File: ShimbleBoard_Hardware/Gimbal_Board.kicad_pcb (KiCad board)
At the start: 2 copper layers, 124.5 x 94 mm, 85 parts, among them Q1 Q_NMOS_GDS, Q2 Q_NMOS_GDS, Q3 Q_NMOS_GDS, Q4 Q_NMOS_GDS, Q5 Q_NMOS_GDS, Q6 Q_NMOS_GDS, Q7 Q_NMOS_GDS, Q8 Q_NMOS_GDS, SW1 SW_Push, SW10 SW_SPDT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

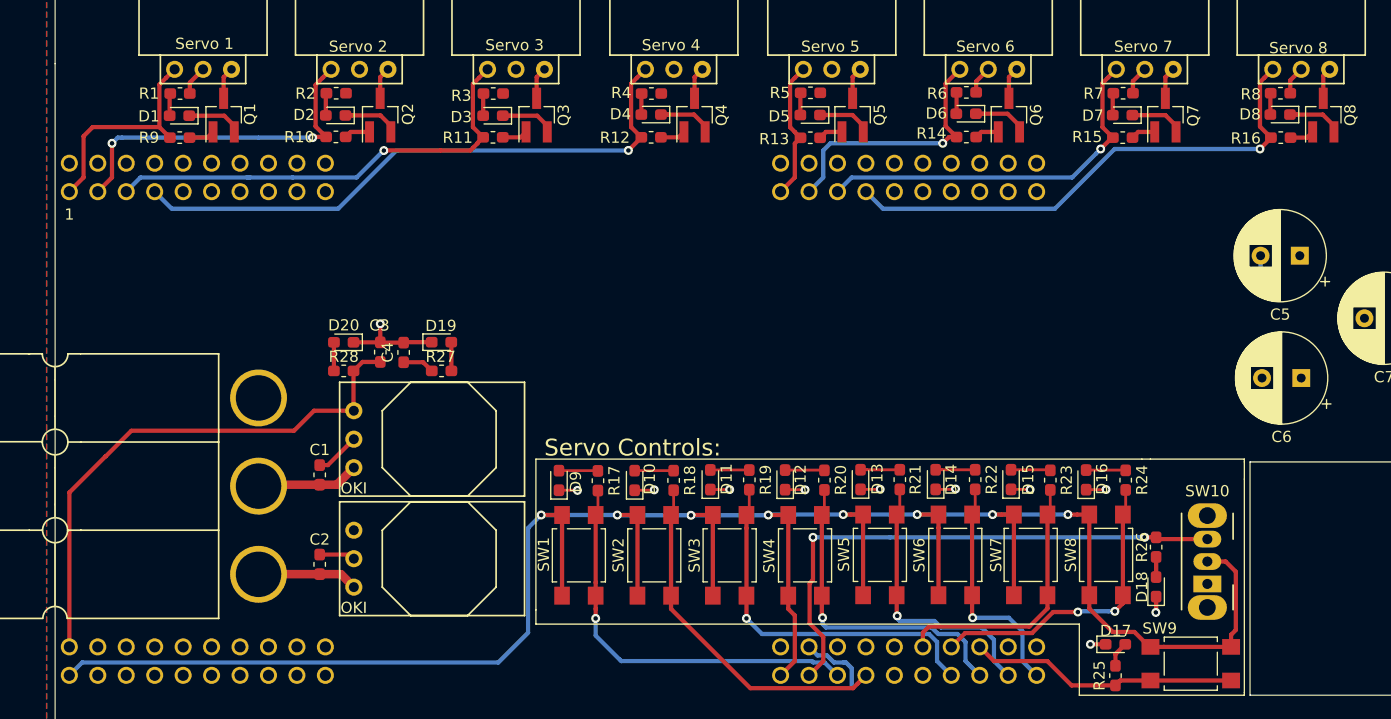
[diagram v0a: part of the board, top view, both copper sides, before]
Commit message: Changed the LED's to 5VL and fixed the wiring for it and added X's
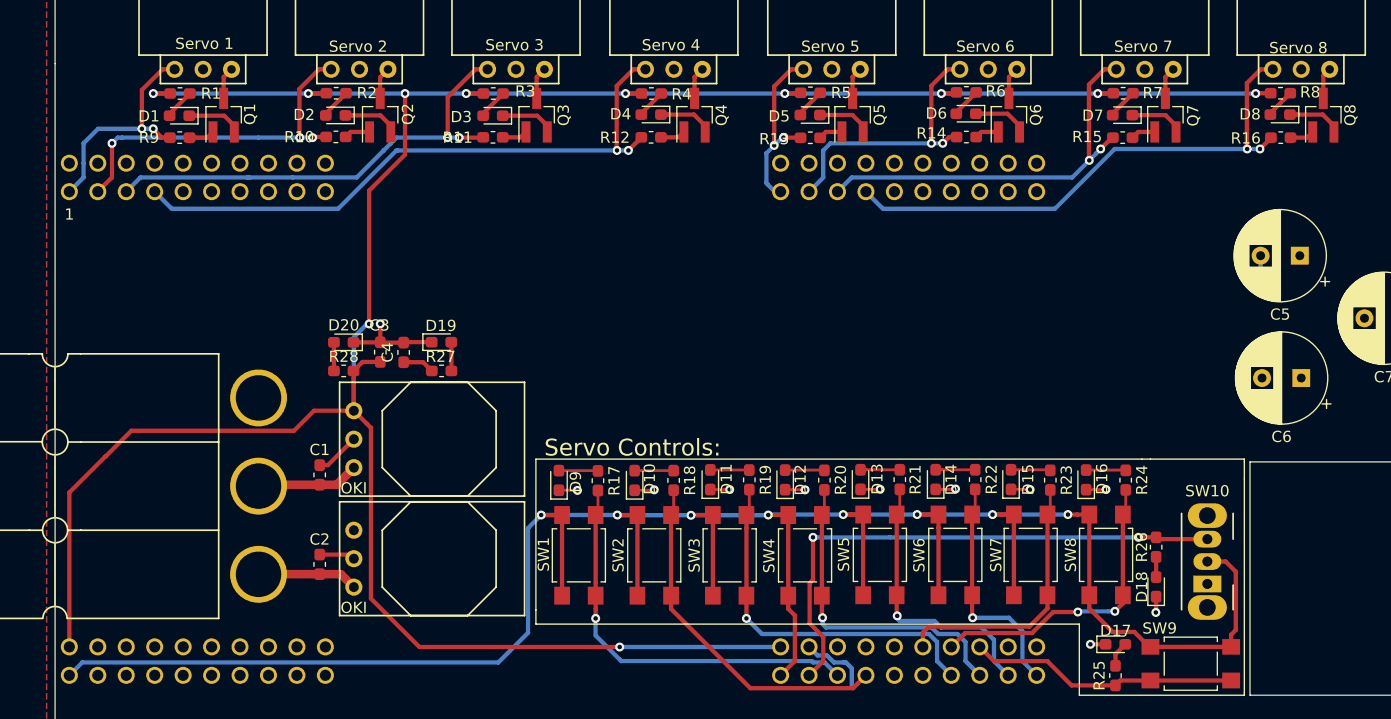
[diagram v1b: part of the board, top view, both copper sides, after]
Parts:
- U1: footprint MRDT_Shields:TM4C129E_Launchpad_FULL_THT_BOTTOM_5 -> MRDT_Shields:TM4C129E_Launchpad_FULL_THT_BOTTOM
- turned R1 to 0 degrees
- turned R2 to 0 degrees
- turned R3 to 0 degrees
- turned R4 to 0 degrees
- turned R5 to 0 degrees
- turned R6 to 0 degrees
- turned R7 to 0 degrees
- turned R8 to 0 degrees
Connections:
- R1 pad 1: +5VA -> +5VL
- R2 pad 1: +5VA -> +5VL
- R3 pad 1: +5VA -> +5VL
- R4 pad 1: +5VA -> +5VL
- R5 pad 1: +5VA -> +5VL
- R6 pad 1: +5VA -> +5VL
- R7 pad 1: +5VA -> +5VL
- R8 pad 1: +5VA -> +5VL
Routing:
- net +5VL: track 48.8 -> 245.1 mm, vias 0 -> 11
- net +5VA: track 13.1 -> 2.84 mm
- net Servo_Ctrl_5: track 12.5 -> 16.4 mm, vias 0 -> 2
- net Servo_Ctrl_7: track 33.6 -> 36.4 mm, vias 1 -> 2
- net Servo_Ctrl_4: track 53.7 -> 55.7 mm, vias 1 -> 2
- net Servo_Ctrl_8: track 46.4 -> 48.2 mm, vias 1 -> 2
- net Servo_Ctrl_6: track 23.6 -> 24.9 mm, vias 1 -> 2
- net Servo_Ctrl_3: track 41.1 -> 42.3 mm, vias 1 -> 2
- net Servo_Ctrl_1: track 19.6 -> 20.6 mm, vias 0 -> 2
- net Servo_Ctrl_2: track 31.2 -> 32.1 mm, vias 2 -> 3
- net Net-(D8-Pad2): track 1.92 -> 2.64 mm
- net Net-(D5-Pad2): track 1.99 -> 2.72 mm
- net Net-(D4-Pad2): track 1.89 -> 2.61 mm
- net Net-(D3-Pad2): track 1.99 -> 2.72 mm
- net Net-(D2-Pad2): track 2.00 -> 2.73 mm
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
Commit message: All but a bit
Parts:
- added D21: 12V_Log_LED, Diode_SMD:D_0603_1608Metric_Pad1.05x0.95mm_HandSolder, F.Cu at (93.2, 69.7)
- added D22: 12V_Act_LED, Diode_SMD:D_0603_1608Metric_Pad1.05x0.95mm_HandSolder, F.Cu at (101.9, 69.6)
- added R29: 1000, Resistor_SMD:R_0603_1608Metric_Pad1.05x0.95mm_HandSolder, F.Cu at (93.1, 72.5)
- added R30: 1000, Resistor_SMD:R_0603_1608Metric_Pad1.05x0.95mm_HandSolder, F.Cu at (101.9, 72.4)
- R17, R18, R19, R20, R21, R22, R23, R24, R25, R26: value 500 -> 330
- U1: footprint MRDT_Shields:TM4C129E_Launchpad_FULL_THT_BOTTOM -> MRDT_Shields:TM4C129E_Launchpad_FULL_THT_BOTTOM_5
- moved C4 1.78 mm to (98.4, 76.1)
- moved C3 1.78 mm to (96.3, 76.0)
- moved D19 1.78 mm to (101.8, 75.2)
- moved D20 1.78 mm to (93.1, 75.2)
- moved R27 1.78 mm to (101.8, 77.7)
- moved R28 1.78 mm to (93.1, 77.7)
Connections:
- Conn1 pad 1: Servo_Ctrl_1 -> +5VA
- Conn1 pad 2: +5VA -> GND
- Conn1 pad 3: GND -> Servo_Ctrl_1
- Conn2 pad 1: Servo_Ctrl_2 -> +5VA
- Conn2 pad 2: +5VA -> GND
- Conn2 pad 3: GND -> Servo_Ctrl_2
- Conn3 pad 1: Servo_Ctrl_3 -> +5VA
- Conn3 pad 2: +5VA -> GND
- Conn3 pad 3: GND -> Servo_Ctrl_3
- Conn4 pad 1: Servo_Ctrl_4 -> +5VA
- Conn4 pad 2: +5VA -> GND
- Conn4 pad 3: GND -> Servo_Ctrl_4
- Conn5 pad 1: Servo_Ctrl_5 -> +5VA
- Conn5 pad 2: +5VA -> GND
- Conn5 pad 3: GND -> Servo_Ctrl_5
- Conn6 pad 1: Servo_Ctrl_6 -> +5VA
- Conn6 pad 2: +5VA -> GND
- Conn6 pad 3: GND -> Servo_Ctrl_6
- Conn7 pad 1: Servo_Ctrl_7 -> +5VA
- Conn7 pad 2: +5VA -> GND
- Conn7 pad 3: GND -> Servo_Ctrl_7
- Conn8 pad 1: Servo_Ctrl_8 -> +5VA
- Conn8 pad 2: +5VA -> GND
- Conn8 pad 3: GND -> Servo_Ctrl_8
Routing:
- net +5VL: track 245.1 -> 191.1 mm, vias 11 -> 10
- net +5VA: track 2.84 -> 40.9 mm, vias 0 -> 9
- net +12VA: track 9.03 -> 44.4 mm, vias 0 -> 1
- net +12L: track 9.55 -> 31.1 mm, vias 0 -> 1
- net GND: track 63.5 -> 76.3 mm, vias 11 -> 14
- net Servo_Ctrl_1: track 20.6 -> 29.0 mm, vias 2 -> 1
- net Servo_Ctrl_3: track 42.3 -> 49.8 mm
- net Servo_Ctrl_4: track 55.7 -> 63.1 mm
- net Servo_Ctrl_2: track 32.1 -> 39.5 mm
- net Servo_Ctrl_7: track 36.4 -> 43.6 mm
- net Servo_Ctrl_8: track 48.2 -> 55.4 mm
- net Servo_Ctrl_6: track 24.9 -> 32.2 mm
- net Servo_Ctrl_5: track 16.4 -> 23.5 mm, vias 2 -> 1
- net Net-(D21-Pad2): track 0.00 -> 3.49 mm
- net Net-(D22-Pad2): track 0.00 -> 3.49 mm
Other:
- board text added: "12V Act"
- board text added: "12V Log"
- board text added: "5V Act"
- board text added: "5V Log"
- board text added: "5VA"
- board text added: "Act/Log Indicators"
- board text added: "GND"
- board text added: "S1"
- board text added: "S2"
- board text added: "S3"
- board text added: "S4"
- board text added: "S5"
- board text added: "S6"
- board text added: "S7"
- board text added: "S8"
- board text added: "Servo's and Indicators"

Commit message: Added signatures
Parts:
- added G***: LOGO, MRDT_Silkscreens:0_MRDT_Logo_20mm, F.Cu at (174.8, 119.6)
- added G***: LOGO, ShimbleBoard_Hardware:Kamran_Winschel_Sig_17.1mmx3.9mm, F.Cu at (97.8, 125.5)
- added G***: LOGO, ShimbleBoard_Hardware:Aaron_Colvin_Sig_4mmx14.1mm, F.Cu at (79.0, 125.5)
- U1: footprint MRDT_Shields:TM4C129E_Launchpad_FULL_THT_BOTTOM_5 -> ShimbleBoard_Hardware:TM4C129E_Launchpad_FULL_THT_BOTTOM_5

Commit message: Different shield
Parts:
- U1: footprint ShimbleBoard_Hardware:TM4C129E_Launchpad_FULL_THT_BOTTOM_5 -> MRDT_Shields:TM4C129E_Launchpad_FULL_THT_BOTTOM
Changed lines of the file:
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@@
     (add_net Servo_Setup_SW)
   )
-  (module ShimbleBoard_Hardware:TM4C129E_Launchpad_FULL_THT_BOTTOM_5 (layer F.Cu)
+  (module MRDT_Shields:TM4C129E_Launchpad_FULL_THT_BOTTOM (layer F.Cu)
     (at 67.31 107.95)
     (fp_text reference U1 (at 122.174 -0.762 180) (layer F.SilkS) hide
@@
       (effects (font (size 1 1) (thickness 0.15)))
     )
-    (fp_line (start 124.46 -55.88) (end 124.46 -68.58) (layer F.Fab) (width 0.15))
-    (fp_line (start -113.2332 -34.163) (end -113.2332 -46.863) (layer F.Fab) (width 0.15))
-    (fp_line (start 0 -55.88) (end 0 -68.58) (layer F.Fab) (width 0.15))
     (fp_line (start 122.428 -20.574) (end 122.428 -20.066) (layer F.Fab) (width 0.05))
     (fp_line (start 124.206 -22.352) (end 124.714 -22.352) (layer F.Fab) (width 0.05))
@@
     )
     (fp_line (start 0 -55.88) (end 0 0.508) (layer F.Fab) (width 0.15))
-    (fp_line (start 0 -68.58) (end 124.46 -68.58) (layer F.Fab) (width 0.15))
+    (fp_line (start 0 -55.88) (end 124.46 -55.88) (layer F.Fab) (width 0.15))
     (fp_line (start 0 0.508) (end 122.428 0.508) (layer F.Fab) (width 0.15))
     (fp_line (start 124.46 -55.88) (end 124.46 -22.352) (layer F.Fab) (width 0.15))
@@
     (pad PM6 thru_hole circle (at 87.63 -46.99 180) (size 1.52 1.52) (drill 1) (layers *.Cu *.Mask F.Paste)
       (net 32 "Net-(U1-PadPM6)"))
-    (pad +3V3 thru_hole circle (at 64.77 -1.27 180) (size 1.52 1.52) (drill 1) (layers *.Cu *.Mask F.Paste)
-      (net 104 +3V3))
+    (pad +3V3` thru_hole circle (at 64.77 -1.27 180) (size 1.52 1.52) (drill 1) (layers *.Cu *.Mask F.Paste))
     (model ${KISYS3DMOD}/Socket_Strips.3dshapes/Socket_Strip_Straight_2x10_Pitch2.54mm.wrl
       (offset (xyz 12.69999980926514 45.71999931335449 -1.904999971389771))

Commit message: Minor changes
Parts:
- added ?: , , F.Cu at (91.9, 85.1)
- added ?: , , F.Cu at (91.9, 81.8)
- added ?: , , F.Cu at (166.4, 91.2)
- Servo Setup: renamed from SW9
- moved C5 57.3 mm to (121.4, 74.7)
- moved C6 35.2 mm to (143.8, 74.7)
- moved C7 19.8 mm to (167.9, 74.9)
- moved SW10 1.78 mm to (170.2, 96.7)
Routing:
- net +3V3: track 206.7 -> 208.5 mm
- net All_Servo_SW: track 48.8 -> 49.6 mm
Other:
- board text added: "5VL"
- board text added: "CCW"
- board text added: "CW"
- board text added: "Servos and Indicators"
- board text removed: "Servo's and Indicators"

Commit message: Wires
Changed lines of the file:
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@@
     (thickness 1.6)
     (drawings 83)
-    (tracks 582)
+    (tracks 580)
     (zones 0)
     (modules 95)
@@
   (segment (start 90.932 97.649) (end 85.485 97.649) (width 0.762) (layer F.Cu) (net 3))
   (segment (start 94.178 77.95) (end 93.952 77.724) (width 0.381) (layer F.Cu) (net 4))
-  (segment (start 93.98 83.058) (end 90.424 83.058) (width 0.381) (layer F.Cu) (net 4))
-  (segment (start 88.636499 84.845501) (end 74.114001 84.845501) (width 0.381) (layer F.Cu) (net 4))
-  (segment (start 90.424 83.058) (end 88.636499 84.845501) (width 0.381) (layer F.Cu) (net 4))
-  (segment (start 74.114001 84.845501) (end 71.837502 87.122) (width 0.381) (layer F.Cu) (net 4))
-  (segment (start 71.837502 87.122) (end 71.8185 87.122) (width 0.381) (layer F.Cu) (net 4))
-  (segment (start 71.8185 87.122) (end 68.58 90.3605) (width 0.381) (layer F.Cu) (net 4))
-  (segment (start 68.58 90.3605) (end 68.58 104.14) (width 0.381) (layer F.Cu) (net 4))
   (segment (start 94.7534 76.9226) (end 93.952 77.724) (width 0.381) (layer F.Cu) (net 4))
   (segment (start 96.3422 76.9226) (end 94.7534 76.9226) (width 0.381) (layer F.Cu) (net 4))
@@
   (segment (start 93.952 83.03) (end 93.98 83.058) (width 0.381) (layer F.Cu) (net 4))
   (segment (start 93.952 77.724) (end 93.952 83.03) (width 0.381) (layer F.Cu) (net 4))
+  (segment (start 68.58 90.678) (end 68.58 104.14) (width 0.381) (layer F.Cu) (net 4))
+  (segment (start 73.406 86.106) (end 68.58 90.678) (width 0.381) (layer F.Cu) (net 4))
+  (segment (start 87.884 86.106) (end 73.406 86.106) (width 0.381) (layer F.Cu) (net 4))
+  (segment (start 93.98 83.058) (end 90.932 83.058) (width 0.381) (layer F.Cu) (net 4))
+  (segment (start 90.932 83.058) (end 87.884 86.106) (width 0.381) (layer F.Cu) (net 4))
   (segment (start 100.1636 76.948) (end 100.9396 77.724) (width 0.381) (layer F.Cu) (net 5))
   (segment (start 98.425 76.948) (end 100.1636 76.948) (width 0.381) (layer F.Cu) (net 5))

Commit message: Stuff
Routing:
- net GND: track 75.8 -> 72.6 mm, vias 14 -> 15
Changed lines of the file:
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@@
     (thickness 1.6)
     (drawings 83)
-    (tracks 580)
+    (tracks 578)
     (zones 0)
     (modules 95)
@@
   )
   (setup
-    (last_trace_width 0.762)
+    (last_trace_width 0.381)
     (user_trace_width 0.381)
     (user_trace_width 0.762)
@@
   (segment (start 102.786999 67.988999) (end 102.743 67.945) (width 0.381) (layer F.Cu) (net 2))
   (segment (start 102.786999 69.596) (end 102.786999 67.988999) (width 0.762) (layer F.Cu) (net 2))
-  (segment (start 138.43 106.045) (end 138.43 107.696) (width 0.381) (layer B.Cu) (net 2))
-  (segment (start 135.379999 104.899999) (end 136.217257 104.899999) (width 0.381) (layer B.Cu) (net 2))
-  (segment (start 134.62 104.14) (end 135.379999 104.899999) (width 0.381) (layer B.Cu) (net 2))
-  (segment (start 136.217257 104.899999) (end 136.906 105.41) (width 0.381) (layer B.Cu) (net 2))
-  (segment (start 136.906 105.41) (end 138.176 105.41) (width 0.381) (layer B.Cu) (net 2))
-  (segment (start 138.176 105.41) (end 138.43 106.045) (width 0.381) (layer B.Cu) (net 2))
   (segment (start 93.613 95.899) (end 93.98 96.266) (width 0.381) (layer F.Cu) (net 2))
   (segment (start 91.299 96.266) (end 90.932 95.899) (width 0.762) (layer F.Cu) (net 2))
   (segment (start 93.98 96.266) (end 91.299 96.266) (width 0.762) (layer F.Cu) (net 2))
+  (segment (start 134.62 103.886) (end 133.93101 103.19701) (width 0.381) (layer F.Cu) (net 2))
+  (segment (start 134.62 104.14) (end 134.62 103.886) (width 0.381) (layer F.Cu) (net 2))
+  (segment (start 133.93101 103.19701) (end 133.93101 102.03499) (width 0.381) (layer F.Cu) (net 2))
+  (via (at 133.604 101.346) (size 0.8) (drill 0.4) (layers F.Cu B.Cu) (net 2))
+  (segment (start 133.93101 102.03499) (end 133.93101 101.67301) (width 0.381) (layer F.Cu) (net 2))
+  (segment (start 133.93101 101.67301) (end 133.604 101.346) (width 0.381) (layer F.Cu) (net 2))
   (segment (start 90.918 97.663) (end 90.932 97.649) (width 0.762) (layer F.Cu) (net 3))
   (segment (start 87.136 97.649) (end 87.122 97.663) (width 0.762) (layer F.Cu) (net 3))
@@
   (via (at 115.57 101.6) (size 0.8) (drill 0.4) (layers F.Cu B.Cu) (net 95))
   (segment (start 115.57 100.749) (end 115.57 101.6) (width 0.381) (layer F.Cu) (net 95))
-  (segment (start 115.57 103.124) (end 115.57 101.6) (width 0.381) (layer B.Cu) (net 95))
   (segment (start 115.7732 92.1648) (end 115.57 92.368) (width 0.25) (layer F.Cu) (net 95))
   (segment (start 115.7732 90.1814) (end 115.7732 92.1648) (width 0.381) (layer F.Cu) (net 95))
-  (segment (start 117.856 105.41) (end 117.729 105.283) (width 0.381) (layer B.Cu) (net 95))
-  (segment (start 117.729 105.283) (end 115.57 103.124) (width 0.381) (layer B.Cu) (net 95))
-  (segment (start 137.16 106.68) (end 136.009499 105.529499) (width 0.381) (layer B.Cu) (net 95))
-  (segment (start 136.009499 105.529499) (end 134.993499 105.529499) (width 0.381) (layer B.Cu) (net 95))
-  (segment (start 134.993499 105.529499) (end 134.874 105.41) (width 0.381) (layer B.Cu) (net 95))
-  (segment (start 134.874 105.41) (end 117.856 105.41) (width 0.381) (layer B.Cu) (net 95))
+  (segment (start 115.57 103.124) (end 115.57 101.6) (width 0.381) (layer B.Cu) (net 95))
+  (segment (start 117.856 105.41) (end 115.57 103.124) (width 0.381) (layer B.Cu) (net 95))
+  (segment (start 137.16 106.68) (end 135.89 105.41) (width 0.381) (layer B.Cu) (net 95))
+  (segment (start 135.89 105.41) (end 117.856 105.41) (width 0.381) (layer B.Cu) (net 95))
   (segment (start 122.301 99.568) (end 122.301 92.368) (width 0.381) (layer F.Cu) (net 96))
   (segment (start 122.5296 92.1394) (end 122.301 92.368) (width 0.25) (layer F.Cu) (net 96))
@@
   (segment (start 132.763 100.749) (end 132.763 99.568) (width 0.381) (layer F.Cu) (net 104))
   (segment (start 132.08 106.68) (end 133.35 105.41) (width 0.381) (layer F.Cu) (net 104))
-  (segment (start 133.35 101.336) (end 132.763 100.749) (width 0.381) (layer F.Cu) (net 104))
-  (segment (start 133.35 105.41) (end 133.35 101.336) (width 0.381) (layer F.Cu) (net 104))
   (segment (start 109.5375 102.87) (end 109.5375 93.5355) (width 0.381) (layer B.Cu) (net 104))
   (segment (start 109.5375 93.5355) (end 110.705 92.368) (width 0.381) (layer B.Cu) (net 104))
@@
   (segment (start 171.811 94.742) (end 172.72 95.651) (width 0.381) (layer F.Cu) (net 104))
   (segment (start 170.18 94.742) (end 171.811 94.742) (width 0.381) (layer F.Cu) (net 104))
+  (segment (start 133.35 105.41) (end 133.35 102.87) (width 0.381) (layer F.Cu) (net 104))
+  (segment (start 132.763 102.283) (end 132.763 100.749) (width 0.381) (layer F.Cu) (net 104))
+  (segment (start 133.35 102.87) (end 132.763 102.283) (width 0.381) (layer F.Cu) (net 104))
   (segment (start 162.639 92.329) (end 162.639 99.529) (width 0.381) (layer F.Cu) (net 106))
   (via (at 161.925 100.965) (size 0.8) (drill 0.4) (layers F.Cu B.Cu) (net 106))
